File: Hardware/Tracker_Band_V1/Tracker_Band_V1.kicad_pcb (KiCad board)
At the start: 4 copper layers, 19.2 x 25.9 mm, 78 parts, among them J1 USB_C_USB20, Q1 SSM6L56FE, SW1 EVP-AVAA1A, SW2 EVP-AVAA1A, U1 ESP32-C3-MINI-1-N4, U2 BNO085, U3 RT8010, U4 MCP73832-2-AC, U5 LM66200, U6 IN-PI15TAT5R5G5B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

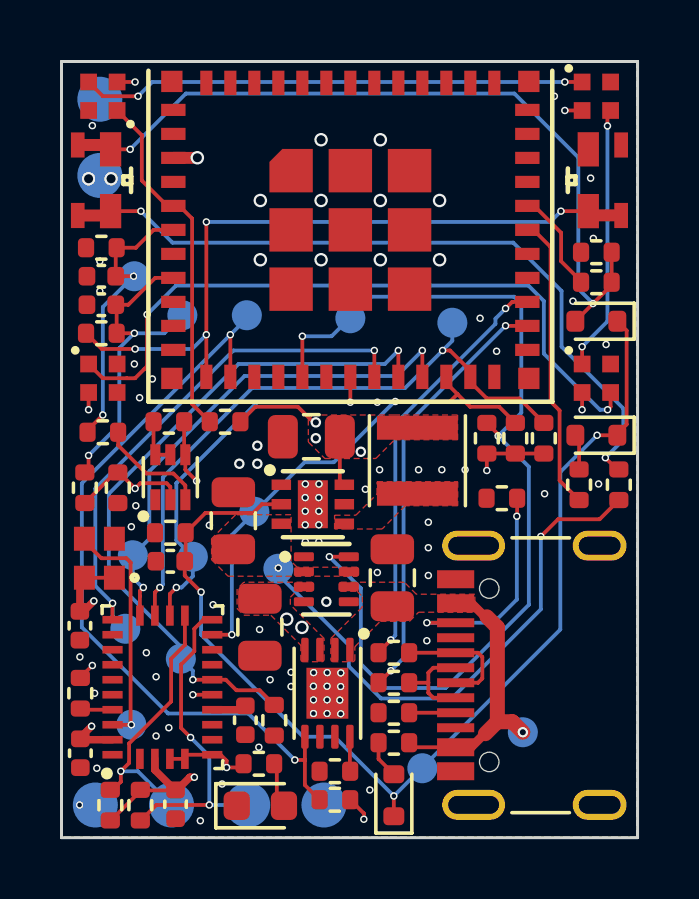
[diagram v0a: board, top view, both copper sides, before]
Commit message: Added SBU to USB C
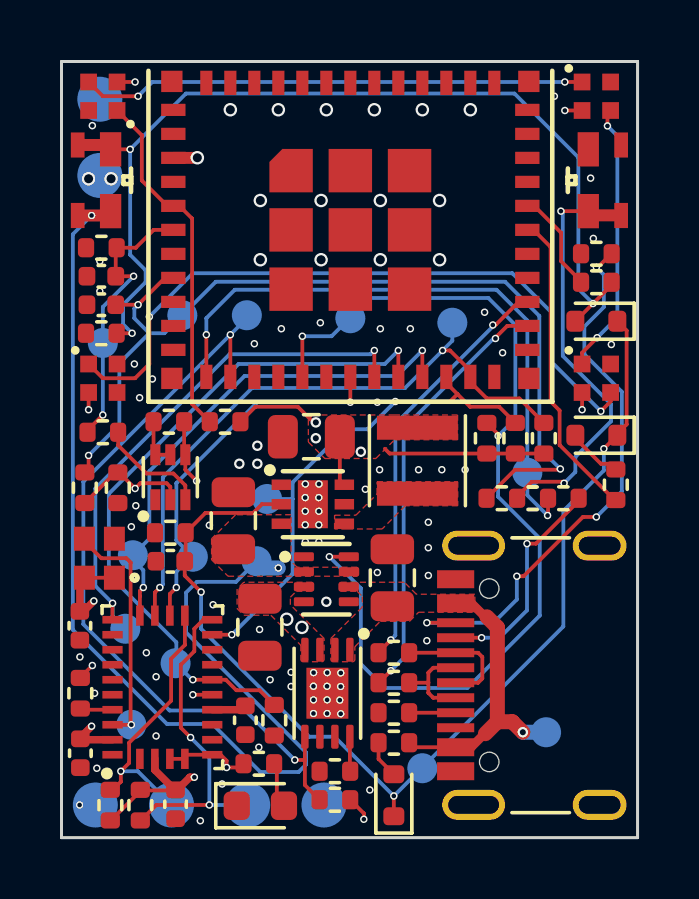
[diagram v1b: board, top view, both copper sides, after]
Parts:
- added TP21: 1mm, TestPoint:TestPoint_Pad_D1.0mm, B.Cu at (137.6, 89.3)
- R17: value 470 -> 1k
- R19, R20: value 100k -> 10k
- moved R19 16.7 mm to (123.4, 84.7)
- moved R24 14.4 mm to (136.8, 90.2), turned to 180 degrees
- moved R7 8.74 mm to (139.9, 82.0)
- moved TP12 2.46 mm to (123.5, 85.0)
- moved R17 1.90 mm to (138.8, 90.2), turned to 180 degrees
- moved R22 1.23 mm to (140.6, 89.7)
- moved TP7 0.78 mm to (138.2, 98.0)
- moved TP8 0.77 mm to (128.6, 92.2)
- moved TP19 0.60 mm to (128.9, 90.2)
- moved TP18 0.23 mm to (125.9, 95.7)
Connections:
- J1 pad A8: unconnected-(J1-SBU1-PadA8) -> /USB_SBU
- R17 pad 1: VCC -> /USB_SBU
- R17 pad 2: Net-(SW1-A) -> /GPIO0
- R24 pad 1: /SW_2 -> /SW2
- SW1 pad 3: Net-(SW1-A) -> VCC
- SW1 pad 4: Net-(SW1-A) -> VCC
- SW2 pad 1: /SW_2 -> /SW2
- SW2 pad 2: /SW_2 -> /SW2
- U1 pad 12: /SW_2 -> /GPIO0
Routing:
- net Net-(SW1-A): track 24.6 -> 0.00 mm, vias 2 -> 0
- net /SW_2: track 23.6 -> 0.00 mm, vias 4 -> 0
- net /GPIO0: track 0.00 -> 20.9 mm, vias 0 -> 2
- net /RST_N: track 11.0 -> 31.6 mm, vias 2 -> 3
- net VCC: track 17.9 -> 36.1 mm
- net /SW2: track 0.00 -> 14.4 mm, vias 0 -> 2
- net Net-(J1-CC2): track 7.66 -> 18.8 mm, vias 2 -> 4
- net /USB_SBU: track 0.00 -> 7.38 mm, vias 0 -> 2
- net /BUCK_EN_SW: track 26.3 -> 32.6 mm, vias 2 -> 3
- net +3.3V: track 28.1 -> 31.0 mm, vias 18 -> 17
- net VBUS: track 9.42 -> 10.2 mm
- net /BNO_INTn: track 16.5 -> 17.2 mm
- net Net-(D4-A): track 1.19 -> 1.88 mm
- net /BUCK_EN_MCU: track 9.84 -> 10.4 mm
- net /BUCK_EN: track 36.1 -> 35.6 mm
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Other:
- board text added: "R"

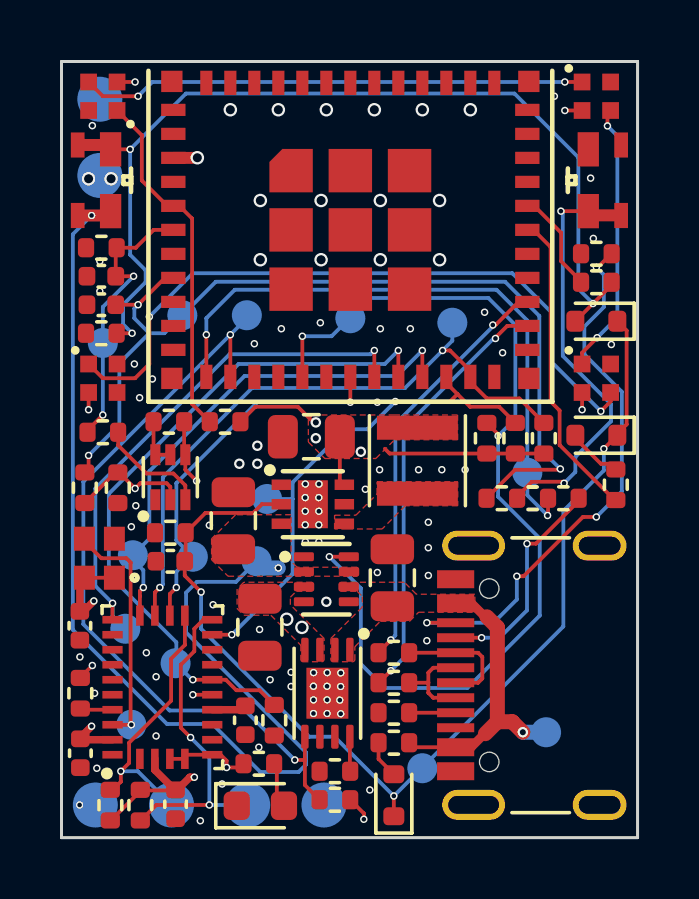
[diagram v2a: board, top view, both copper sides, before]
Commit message: Vias updated to plugged 0.3mm & Gerbers Finalized
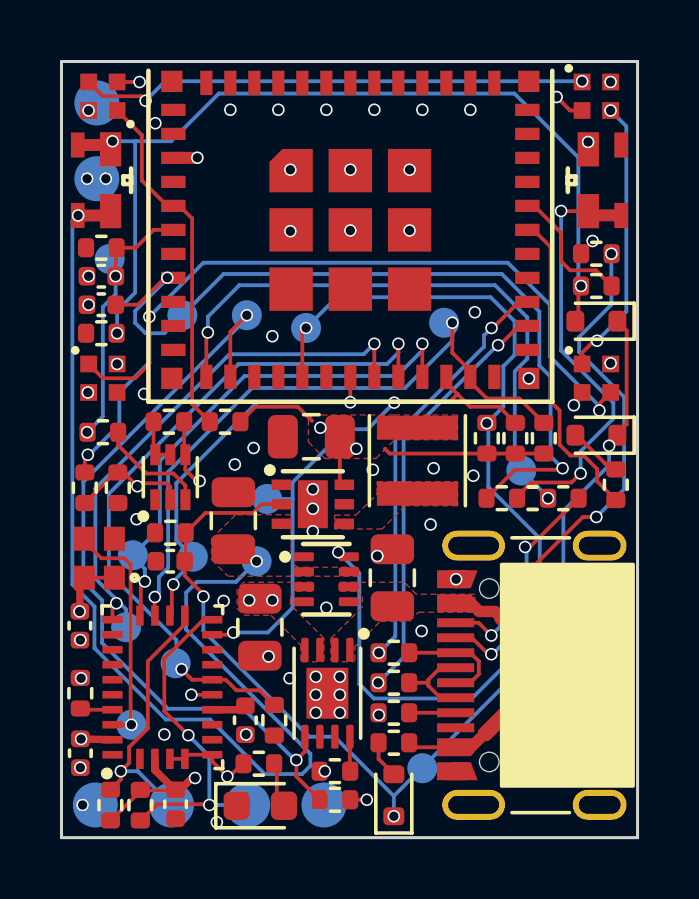
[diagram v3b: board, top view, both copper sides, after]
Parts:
- moved TP12 2.81 mm to (123.7, 82.2)
- moved TP10 1.51 mm to (130.2, 84.5)
- moved TP17 0.28 mm to (134.8, 84.3)
- moved TP21 0.21 mm to (137.4, 89.2)
- moved TP6 0.16 mm to (123.2, 77.0)
- moved TP5 0.15 mm to (123.2, 79.5)
- moved R20 0.12 mm to (139.9, 83.1), turned to 0 degrees
- moved TP15 0.06 mm to (124.2, 94.5)
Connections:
- net Net-(D3-A) renamed /PWR_AN
- net Net-(J1-CC1) renamed /USB_CC1
- net Net-(J1-CC2) renamed /USB_CC2
- net Net-(J1-D+-PadA6) renamed /D+
- net Net-(J1-D--PadA7) renamed /D-
- net Net-(Q1A-D) renamed /PFET_G
- net Net-(Q1B-D) renamed /PFET_D
- net Net-(U2-CAP) renamed /BNO_CAP
- net Net-(U4-PROG) renamed /CHRG_PROG
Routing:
- net /RST_N: track 31.6 -> 33.6 mm
- net /BUCK_EN_SW: track 32.6 -> 30.9 mm
- net VBUS: track 10.2 -> 11.8 mm
- net +3.3V: track 31.0 -> 29.5 mm, vias 17 -> 16
- net /USB_CC2: track 18.8 -> 17.5 mm
- net /SW_1: track 3.42 -> 4.56 mm
- net /CHRG_ST: track 25.5 -> 26.5 mm
- net VCC: track 36.1 -> 35.3 mm
- net /BNO_INTn: track 17.2 -> 17.9 mm
- net /OR_ST: track 32.4 -> 33.1 mm
- net /USB_SBU: track 7.38 -> 8.05 mm
- net /BNO_CSn: track 21.5 -> 22.1 mm
- net /GPIO0: track 20.9 -> 20.3 mm
- net GND: track 0.15 -> 0.31 mm, vias 86 -> 55

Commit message: Component ordering information finalized
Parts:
- R17: value 1k -> 330
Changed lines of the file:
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@@
         (effects (font (size 1 1) (thickness 0.15)))
     )
-    (fp_text value "1k" (at 0 -0.55) (layer "F.Fab")
+    (fp_text value "330" (at 0 -0.55) (layer "F.Fab")
         (effects (font (size 0.3 0.3) (thickness 0.05) bold))
     )
@@
     (property "Sheetfile" "Tracker_Band_V1.kicad_sch")
     (property "Sheetname" "")
+    (property "exclude_from_bom" "")
     (property "ki_description" "test point")
     (property "ki_keywords" "test point tp")
-    (attr exclude_from_pos_files)
+    (attr exclude_from_pos_files exclude_from_bom)
     (fp_text reference "TP9" (at 0 1.448) (layer "B.SilkS") hide
         (effects (font (size 1 1) (thickness 0.15)) (justify mirror))
@@
     (property "Sheetfile" "Tracker_Band_V1.kicad_sch")
     (property "Sheetname" "")
+    (property "exclude_from_bom" "")
     (property "ki_description" "test point")
     (property "ki_keywords" "test point tp")
-    (attr exclude_from_pos_files)
+    (attr exclude_from_pos_files exclude_from_bom)
     (fp_text reference "TP20" (at 0 1.448) (layer "B.SilkS") hide
         (effects (font (size 1 1) (thickness 0.15)) (justify mirror))
@@
     (property "Sheetfile" "Tracker_Band_V1.kicad_sch")
     (property "Sheetname" "")
+    (property "exclude_from_bom" "")
     (property "ki_description" "test point")
     (property "ki_keywords" "test point tp")
-    (attr exclude_from_pos_files)
+    (attr exclude_from_pos_files exclude_from_bom)
     (fp_text reference "TP11" (at 0 1.448) (layer "B.SilkS") hide
         (effects (font (size 1 1) (thickness 0.15)) (justify mirror))
@@
     (property "Sheetfile" "Tracker_Band_V1.kicad_sch")
     (property "Sheetname" "")
+    (property "exclude_from_bom" "")
     (property "ki_description" "test point")
     (property "ki_keywords" "test point tp")
-    (attr exclude_from_pos_files)
+    (attr exclude_from_pos_files exclude_from_bom)
     (fp_text reference "TP8" (at 0 1.448) (layer "B.SilkS") hide
         (effects (font (size 1 1) (thickness 0.15)) (justify mirror))
@@
     (property "Sheetfile" "Tracker_Band_V1.kicad_sch")
     (property "Sheetname" "")
+    (property "exclude_from_bom" "")
     (property "ki_description" "test point")
     (property "ki_keywords" "test point tp")
-    (attr exclude_from_pos_files)
+    (attr exclude_from_pos_files exclude_from_bom)
     (fp_text reference "TP3" (at 0 1.648) (layer "B.SilkS") hide
         (effects (font (size 1 1) (thickness 0.15)) (justify mirror))
@@
     (property "Sheetfile" "Tracker_Band_V1.kicad_sch")
     (property "Sheetname" "")
+    (property "exclude_from_bom" "")
     (property "ki_description" "test point")
     (property "ki_keywords" "test point tp")
-    (attr exclude_from_pos_files)
+    (attr exclude_from_pos_files exclude_from_bom)
     (fp_text reference "TP5" (at 0 1.648) (layer "B.SilkS") hide
         (effects (font (size 1 1) (thickness 0.15)) (justify mirror))
@@
     (property "Sheetfile" "Tracker_Band_V1.kicad_sch")
     (property "Sheetname" "")
+    (property "exclude_from_bom" "")
     (property "ki_description" "test point")
     (property "ki_keywords" "test point tp")
-    (attr exclude_from_pos_files)
+    (attr exclude_from_pos_files exclude_from_bom)
     (fp_text reference "TP21" (at 0 1.448) (layer "B.SilkS") hide
         (effects (font (size 1 1) (thickness 0.15)) (justify mirror))
@@
     (property "Sheetfile" "Tracker_Band_V1.kicad_sch")
     (property "Sheetname" "")
+    (property "exclude_from_bom" "")
     (property "ki_description" "test point")
     (property "ki_keywords" "test point tp")
-    (attr exclude_from_pos_files)
+    (attr exclude_from_pos_files exclude_from_bom)
     (fp_text reference "TP16" (at 0 1.448) (layer "B.SilkS") hide
         (effects (font (size 1 1) (thickness 0.15)) (justify mirror))
@@
     (property "Sheetfile" "Tracker_Band_V1.kicad_sch")
     (property "Sheetname" "")
+    (property "exclude_from_bom" "")
     (property "ki_description" "test point")
     (property "ki_keywords" "test point tp")
-    (attr exclude_from_pos_files)
+    (attr exclude_from_pos_files exclude_from_bom)
     (fp_text reference "TP6" (at 0 1.648) (layer "B.SilkS") hide
         (effects (font (size 1 1) (thickness 0.15)) (justify mirror))
@@
     (property "Sheetfile" "Tracker_Band_V1.kicad_sch")
     (property "Sheetname" "")
+    (property "exclude_from_bom" "")
     (property "ki_description" "test point")
     (property "ki_keywords" "test point tp")
-    (attr exclude_from_pos_files)
+    (attr exclude_from_pos_files exclude_from_bom)
     (fp_text reference "TP7" (at 0 1.448) (layer "B.SilkS") hide
         (effects (font (size 1 1) (thickness 0.15)) (justify mirror))
@@
     (property "Sheetfile" "Tracker_Band_V1.kicad_sch")
     (property "Sheetname" "")
+    (property "exclude_from_bom" "")
     (property "ki_description" "test point")
     (property "ki_keywords" "test point tp")
-    (attr exclude_from_pos_files)
+    (attr exclude_from_pos_files exclude_from_bom)
     (fp_text reference "TP15" (at 0 1.448) (layer "B.SilkS") hide
         (effects (font (size 1 1) (thickness 0.15)) (justify mirror))
@@
     (property "Sheetfile" "Tracker_Band_V1.kicad_sch")
     (property "Sheetname" "")
+    (property "exclude_from_bom" "")
     (property "ki_description" "test point")
     (property "ki_keywords" "test point tp")
-    (attr exclude_from_pos_files)
+    (attr exclude_from_pos_files exclude_from_bom)
     (fp_text reference "TP4" (at 0 1.648) (layer "B.SilkS") hide
         (effects (font (size 1 1) (thickness 0.15)) (justify mirror))
@@
     (property "Sheetfile" "Tracker_Band_V1.kicad_sch")
     (property "Sheetname" "")
+    (property "exclude_from_bom" "")
     (property "ki_description" "test point")
     (property "ki_keywords" "test point tp")
-    (attr exclude_from_pos_files)
+    (attr exclude_from_pos_files exclude_from_bom)
     (fp_text reference "TP12" (at 0 1.448) (layer "B.SilkS") hide
         (effects (font (size 1 1) (thickness 0.15)) (justify mirror))
@@
     (property "Sheetfile" "Tracker_Band_V1.kicad_sch")
     (property "Sheetname" "")
+    (property "exclude_from_bom" "")
     (property "ki_description" "test point")
     (property "ki_keywords" "test point tp")
-    (attr exclude_from_pos_files)
+    (attr exclude_from_pos_files exclude_from_bom)
     (fp_text reference "TP14" (at 0 1.448) (layer "B.SilkS") hide
         (effects (font (size 1 1) (thickness 0.15)) (justify mirror))
@@
     (property "Sheetfile" "Tracker_Band_V1.kicad_sch")
     (property "Sheetname" "")
+    (property "exclude_from_bom" "")
     (property "ki_description" "test point")
     (property "ki_keywords" "test point tp")
-    (attr exclude_from_pos_files)
+    (attr exclude_from_pos_files exclude_from_bom)
     (fp_text reference "TP10" (at 0 1.448) (layer "B.SilkS") hide
         (effects (font (size 1 1) (thickness 0.15)) (justify mirror))
@@
     (property "Sheetfile" "Tracker_Band_V1.kicad_sch")
     (property "Sheetname" "")
+    (property "exclude_from_bom" "")
     (property "ki_description" "test point")
     (property "ki_keywords" "test point tp")
-    (attr exclude_from_pos_files)
+    (attr exclude_from_pos_files exclude_from_bom)
     (fp_text reference "TP18" (at 0 1.448) (layer "B.SilkS") hide
         (effects (font (size 1 1) (thickness 0.15)) (justify mirror))
@@
     (property "Sheetfile" "Tracker_Band_V1.kicad_sch")
     (property "Sheetname" "")
+    (property "exclude_from_bom" "")
     (property "ki_description" "test point")
     (property "ki_keywords" "test point tp")
-    (attr exclude_from_pos_files)
+    (attr exclude_from_pos_files exclude_from_bom)
     (fp_text reference "TP19" (at 0 1.448) (layer "B.SilkS") hide
         (effects (font (size 1 1) (thickness 0.15)) (justify mirror))
@@
     (property "Sheetfile" "Tracker_Band_V1.kicad_sch")
     (property "Sheetname" "")
+    (property "exclude_from_bom" "")
     (property "ki_description" "test point")
     (property "ki_keywords" "test point tp")
-    (attr exclude_from_pos_files)
+    (attr exclude_from_pos_files exclude_from_bom)
     (fp_text reference "TP17" (at 0 1.448) (layer "B.SilkS") hide
         (effects (font (size 1 1) (thickness 0.15)) (justify mirror))
@@
     (property "Sheetfile" "Tracker_Band_V1.kicad_sch")
     (property "Sheetname" "")
+    (property "exclude_from_bom" "")
     (property "ki_description" "test point")
     (property "ki_keywords" "test point tp")
-    (attr exclude_from_pos_files)
+    (attr exclude_from_pos_files exclude_from_bom)
     (fp_text reference "TP13" (at 0 1.448) (layer "B.SilkS") hide
         (effects (font (size 1 1) (thickness 0.15)) (justify mirror))
@@
     (property "Sheetfile" "Tracker_Band_V1.kicad_sch")
     (property "Sheetname" "")
-    (attr board_only exclude_from_pos_files)
+    (property "exclude_from_bom" "")
+    (attr board_only exclude_from_pos_files exclude_from_bom)
     (fp_text reference "LG1" (at 0 0) (layer "B.SilkS") hide
         (effects (font (size 1.5 1.5) (thickness 0.3)) (justify mirror))
@@
     (property "Sheetfile" "Tracker_Band_V1.kicad_sch")
     (property "Sheetname" "")
+    (property "exclude_from_bom" "")
     (property "ki_description" "test point")
     (property "ki_keywords" "test point tp")
-    (attr exclude_from_pos_files)
+    (attr exclude_from_pos_files exclude_from_bom)
     (fp_text reference "TP2" (at 0 1.648) (layer "B.SilkS") hide
         (effects (font (size 1 1) (thickness 0.15)) (justify mirror))
@@
     (property "Sheetfile" "Tracker_Band_V1.kicad_sch")
     (property "Sheetname" "")
+    (property "exclude_from_bom" "")
     (property "ki_description" "test point")
     (property "ki_keywords" "test point tp")
-    (attr exclude_from_pos_files)
+    (attr exclude_from_pos_files exclude_from_bom)
     (fp_text reference "TP1" (at 0 1.648) (layer "B.SilkS") hide
         (effects (font (size 1 1) (thickness 0.15)) (justify mirror))
